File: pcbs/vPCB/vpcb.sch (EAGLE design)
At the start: 39 parts

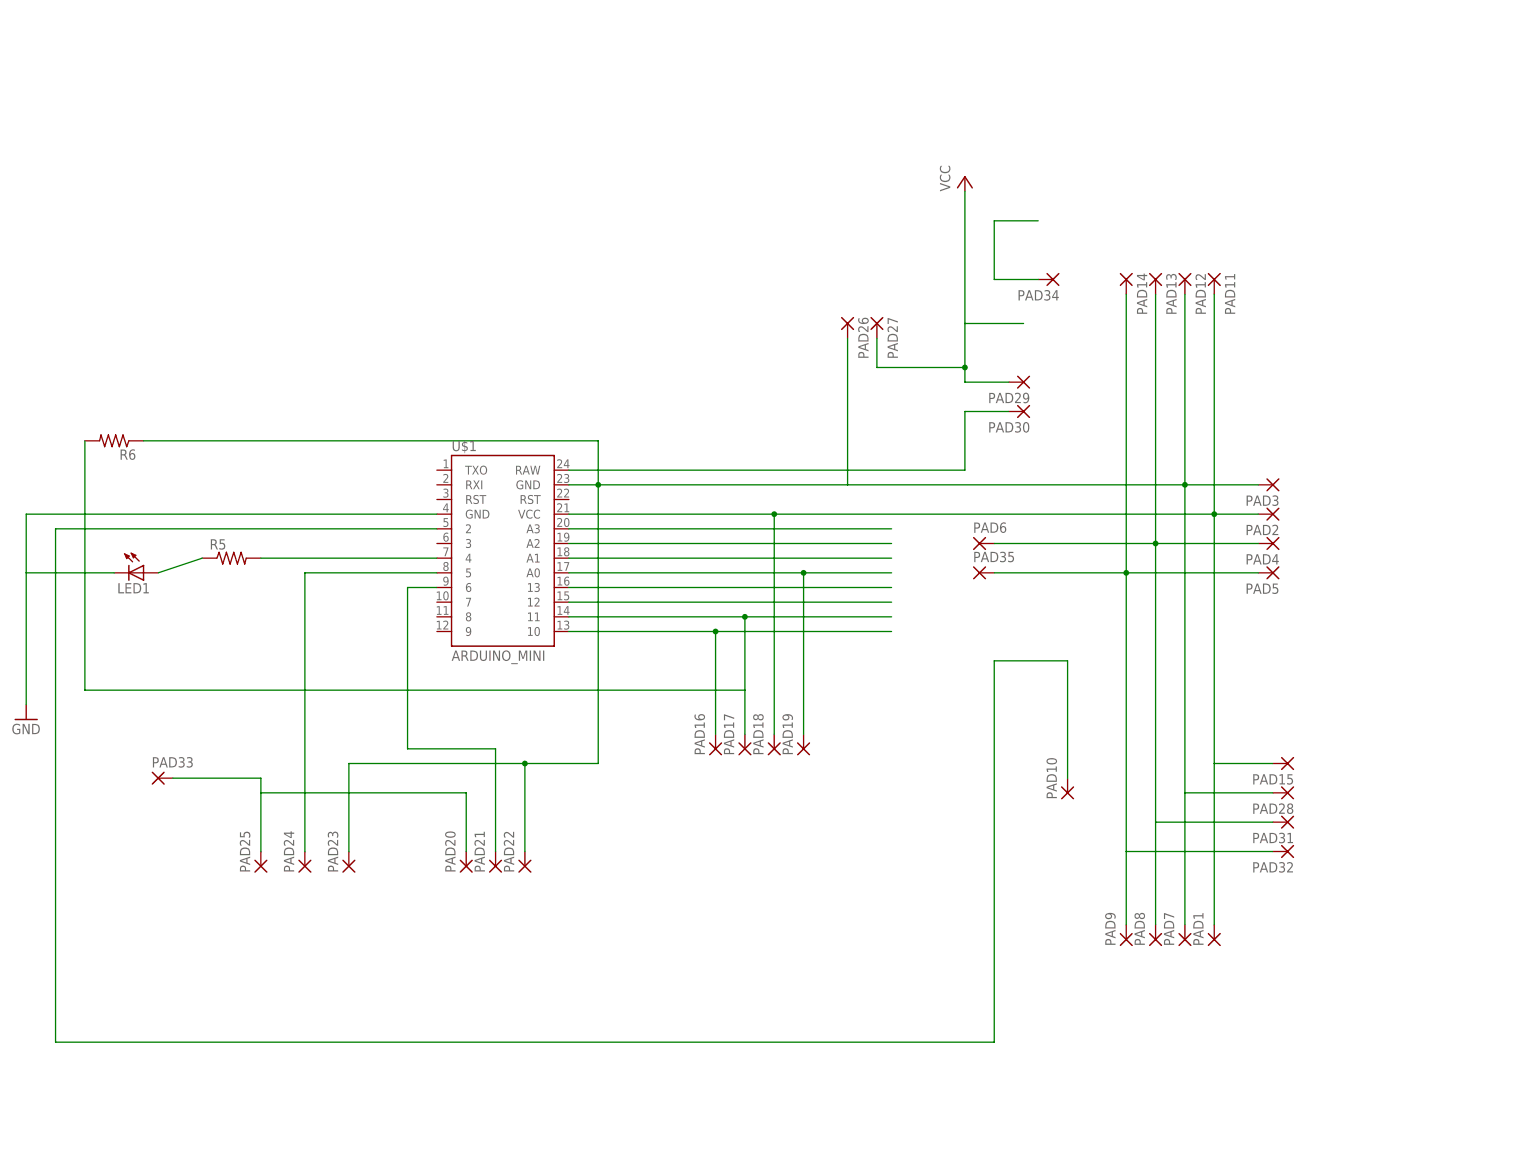
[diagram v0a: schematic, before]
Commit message: * Making PCM a bit wider to accomodate battery.
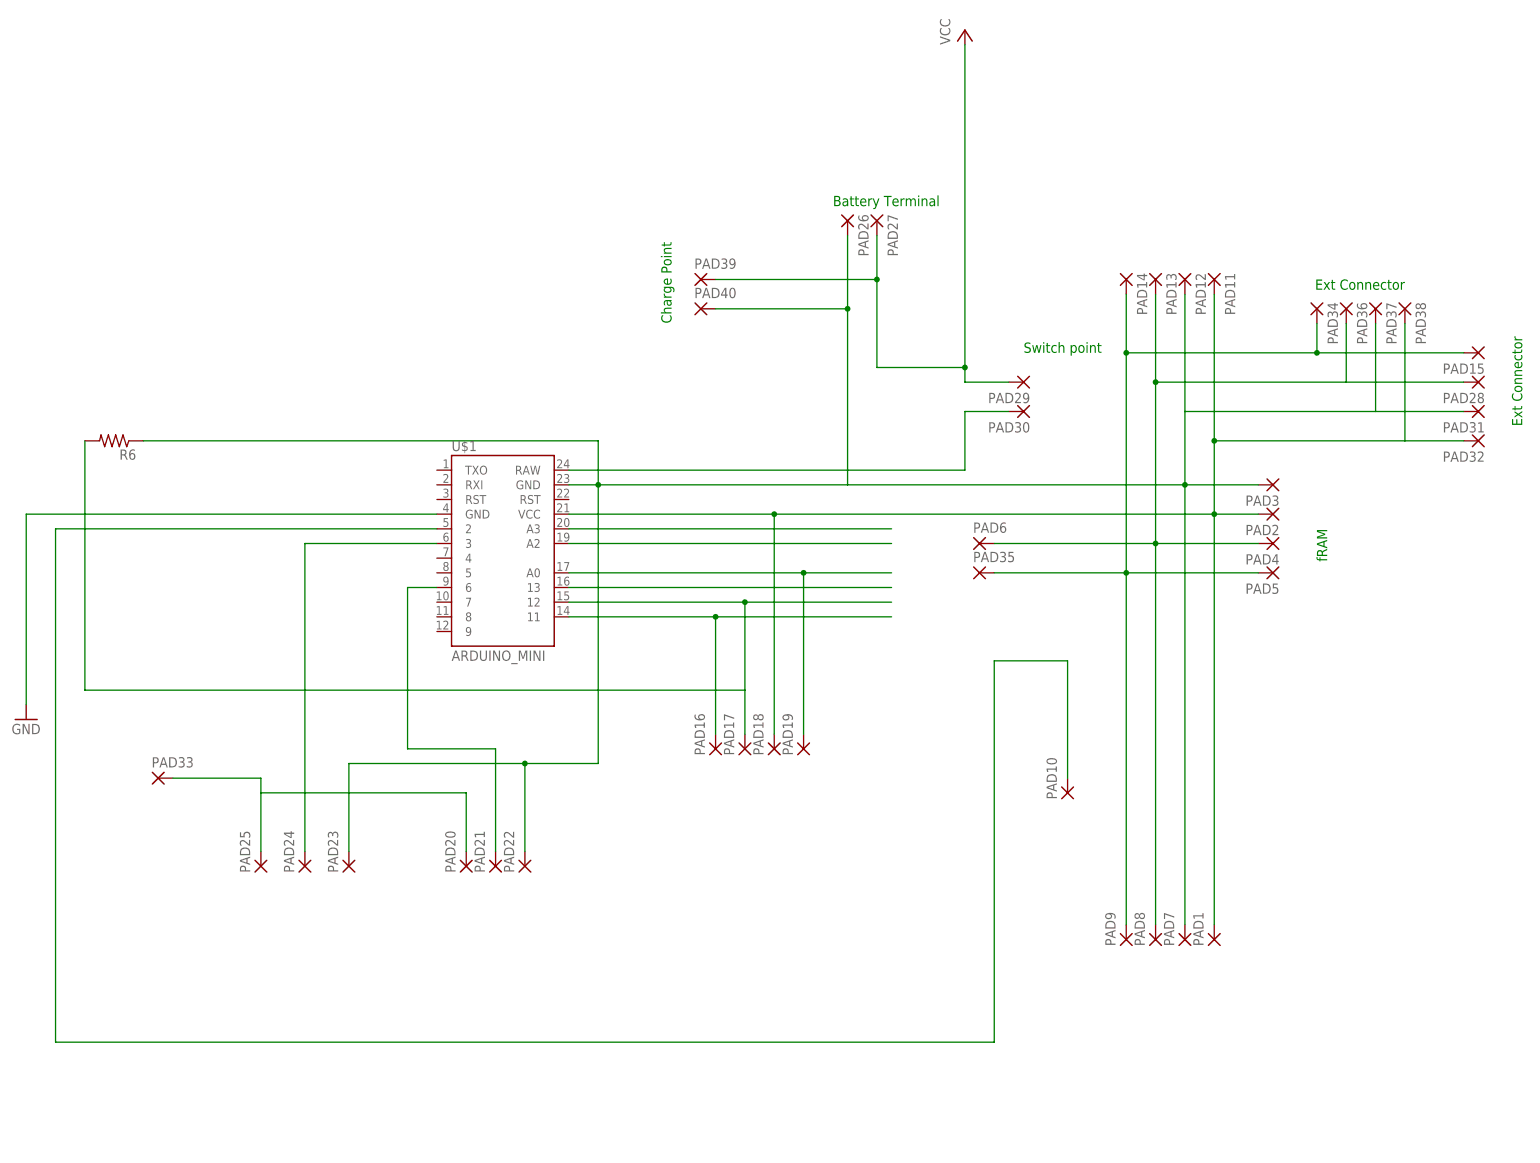
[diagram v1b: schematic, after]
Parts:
- removed LED1: (no value), led:LED3MM
- removed R5: (no value), resistor:R-US_0204/5
- added PAD36, PAD37, PAD38, PAD39, PAD40: (no value), wirepad:2,15/1,0
- U$1: device Joe_SparkFun-Boards:ARDUINO_MINI -> vPCB_Joe_SparkFun-Boards:ARDUINO_MINI
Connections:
- removed net N$11: U$1.A1
- removed net N$13: U$1.12
- removed net N$16: LED1.A, R5.1
- removed net N$18: PAD34.P
- removed net N$23: R5.2, U$1.4
- removed net N$4: PAD16.P, U$1.10
- new net N$20: PAD16.P, U$1.11
- net GND: no longer LED1.C
- net N$1: now also PAD28.P, PAD36.P; no longer PAD31.P
- net N$14: now also U$1.3; no longer U$1.5
- net N$17: now also U$1.12; no longer U$1.11
- net N$19: now also PAD31.P, PAD37.P, PAD40.P; no longer PAD28.P
- net N$2: now also PAD15.P, PAD34.P; no longer PAD32.P
- net N$3: now also PAD32.P, PAD38.P; no longer PAD15.P
- net VCC: now also PAD39.P
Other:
- note added: "Battery Terminal"
- note added: "Charge Point"
- note added: "Ext Connector"
- note added: "Switch point"
- note added: "fRAM"
- moved on the sheet: PAD15, PAD26, PAD27, PAD28, PAD31, PAD32, PAD34

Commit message: Many refinements to vPCB. - Adding ID, date build - Adding charge point - Adding LED - Adding voltage-test resistors - Fixing battery connector (was around the wrong way) - Adding sufficient space (top/bottom) to slip into 1.5mm trench.
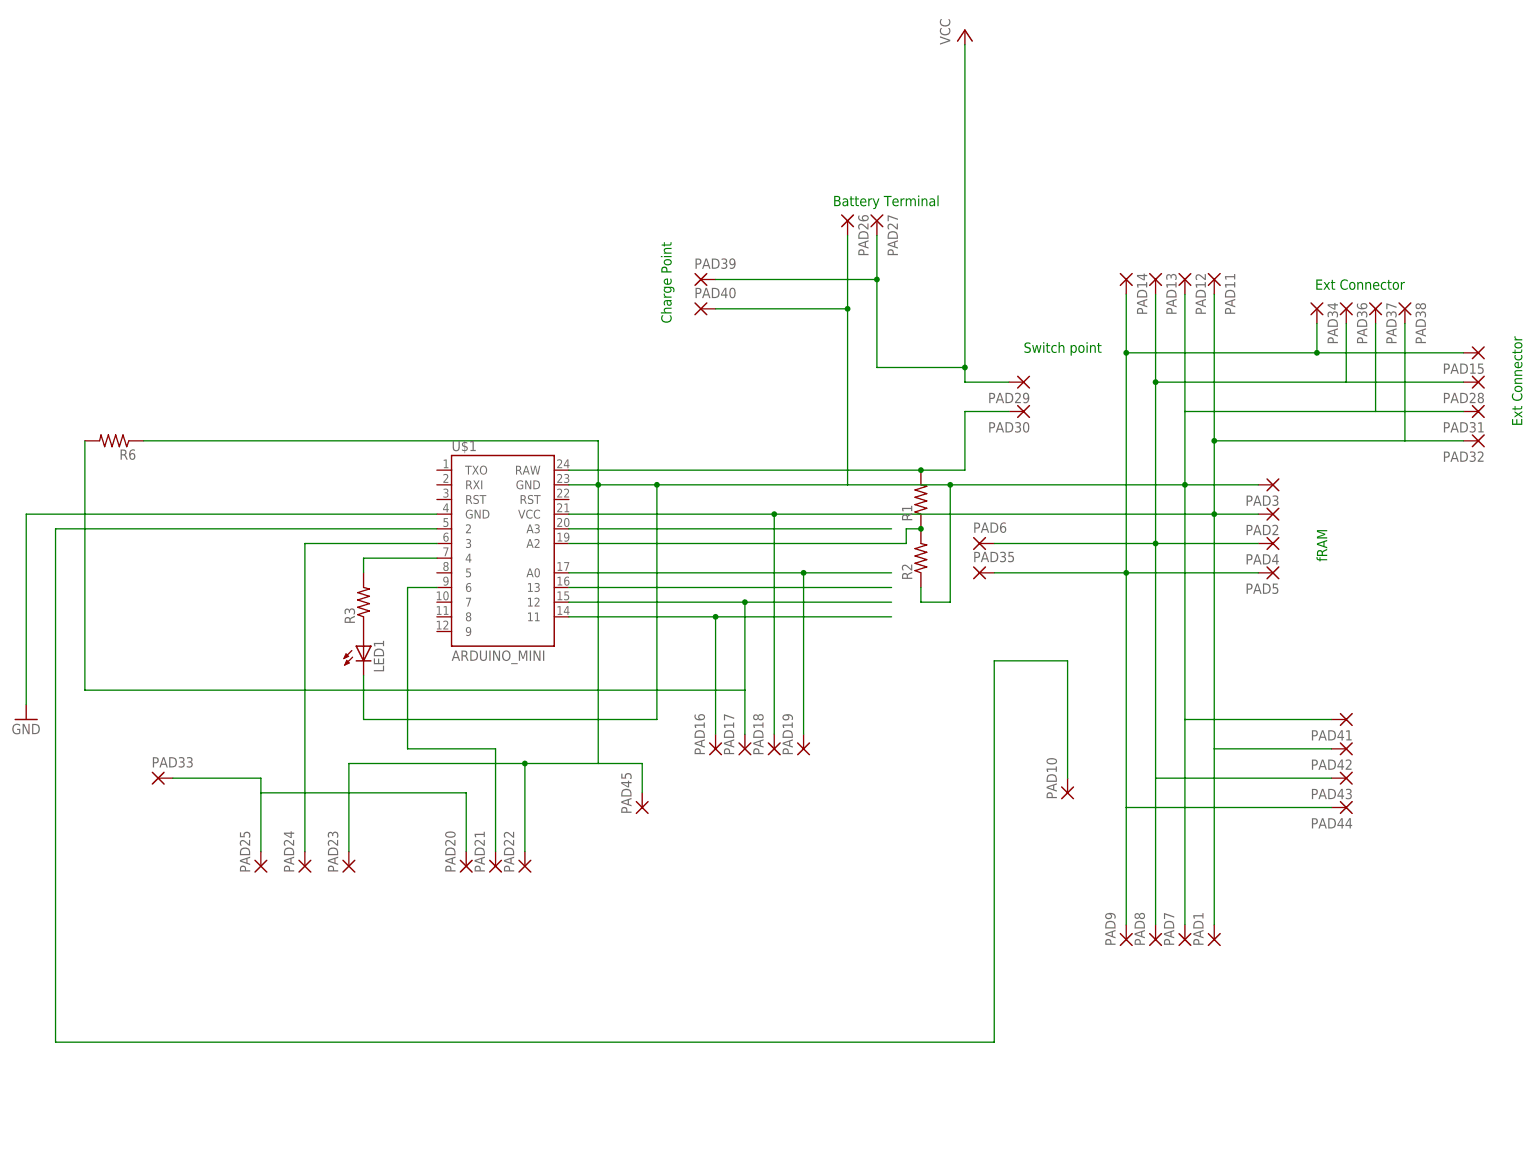
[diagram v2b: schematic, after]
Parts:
- added LED1: (no value), led:LED3MM
- added PAD41, PAD42, PAD43, PAD44, PAD45: (no value), wirepad:2,15/1,0
- added R1, R2, R3: (no value), resistor:R-US_0204/7
- PAD35, PAD6: device wirepad:1,6/0,8 -> wirepad:2,15/1,0
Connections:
- removed net N$19: PAD12.P, PAD22.P, PAD23.P, PAD26.P, PAD3.P, PAD31.P, PAD37.P, PAD40.P, PAD7.P, R6.1, U$1.GND@2
- new net N$11: LED1.A, R3.1
- new net N$13: R3.2, U$1.4
- new net N$16: LED1.C, PAD12.P, PAD22.P, PAD23.P, PAD26.P, PAD3.P, PAD31.P, PAD37.P, PAD40.P, PAD41.P, PAD45.P, PAD7.P, R2.1, R6.1, U$1.GND@2
- net N$1: now also PAD43.P
- net N$10: now also R1.1, R2.2
- net N$2: now also PAD44.P
- net N$3: now also PAD42.P
- net N$5: now also R1.2

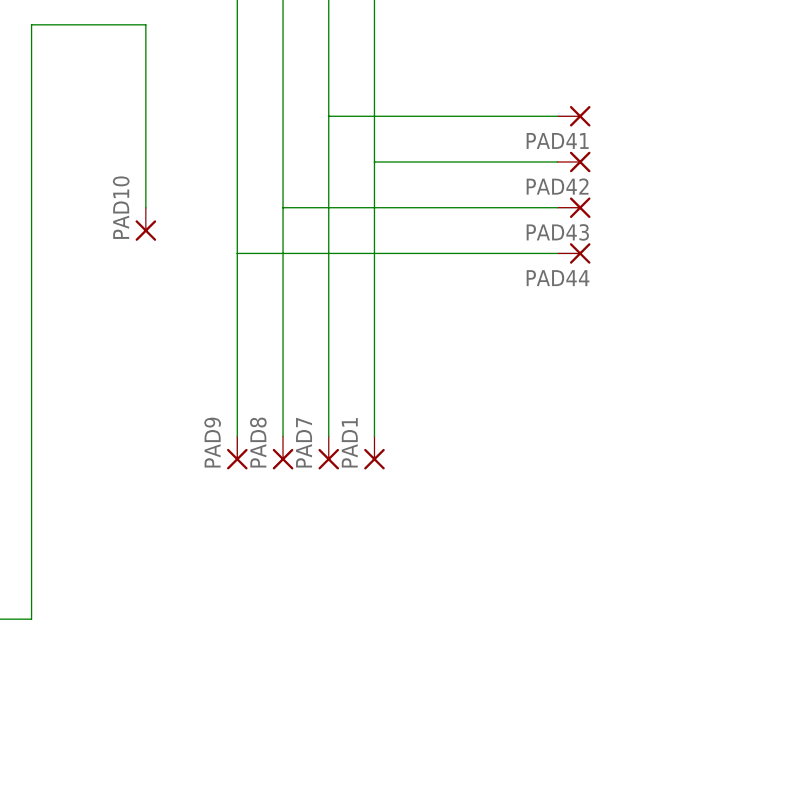
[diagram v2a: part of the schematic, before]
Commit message: * Resolved issue with Air sensor pin arrangement not compatible with vPCB * Resolved issue with Servo +ve and Signal being around the wrong way
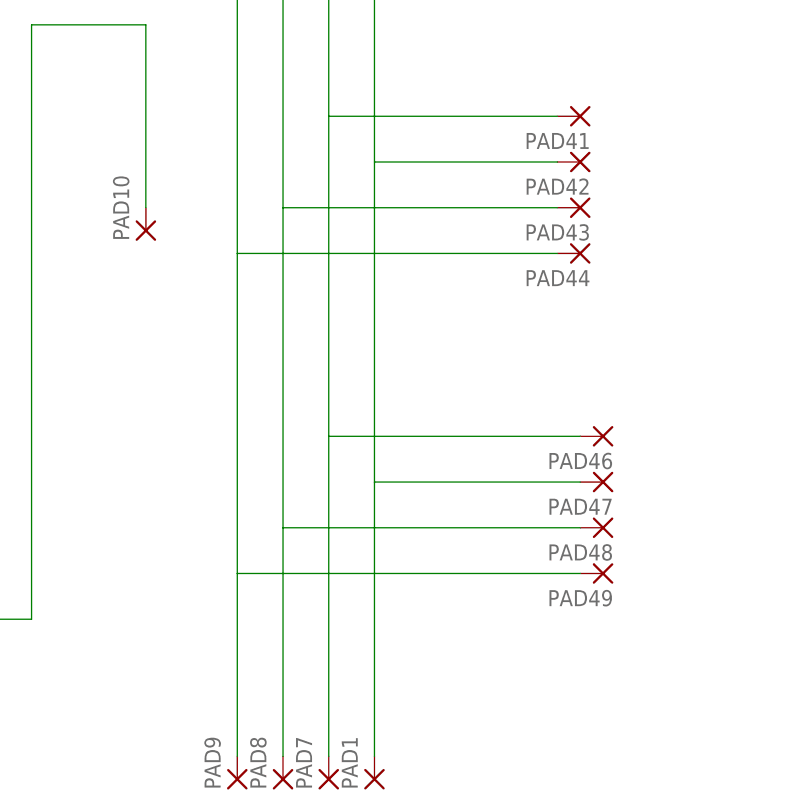
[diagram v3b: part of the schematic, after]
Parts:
- added PAD46, PAD47, PAD48, PAD49: (no value), wirepad:2,15/1,0
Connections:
- net N$1: now also PAD48.P
- net N$16: now also PAD46.P
- net N$2: now also PAD49.P
- net N$3: now also PAD47.P
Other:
- moved on the sheet: PAD1, PAD7, PAD8, PAD9
